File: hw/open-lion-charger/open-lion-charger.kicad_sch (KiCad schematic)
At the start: 5 parts

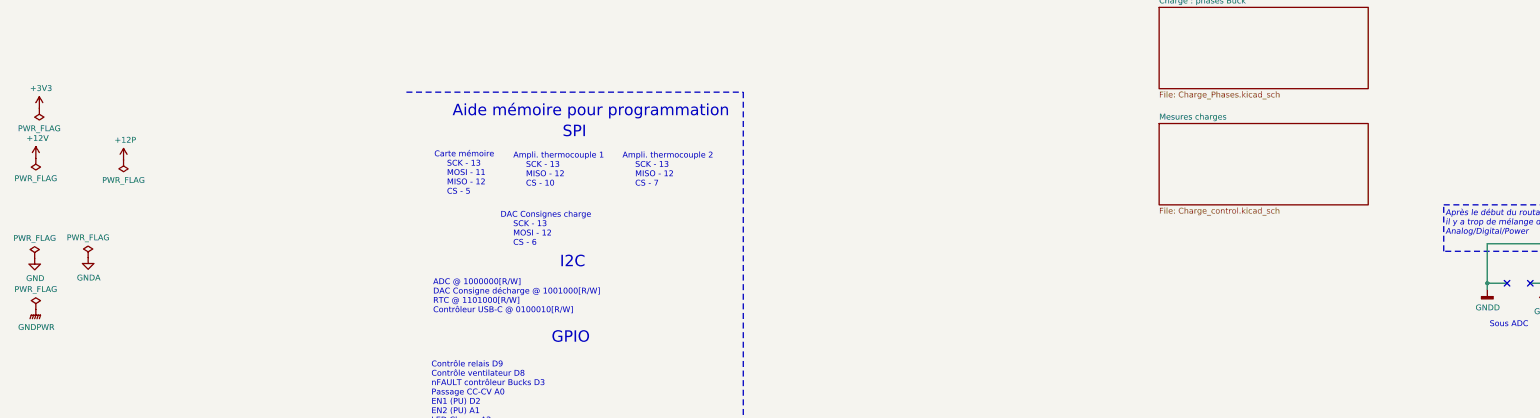
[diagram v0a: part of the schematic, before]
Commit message: Done with PCB review
Warning : issue with net +12P and confusion with RELAIS_BATT_OUT
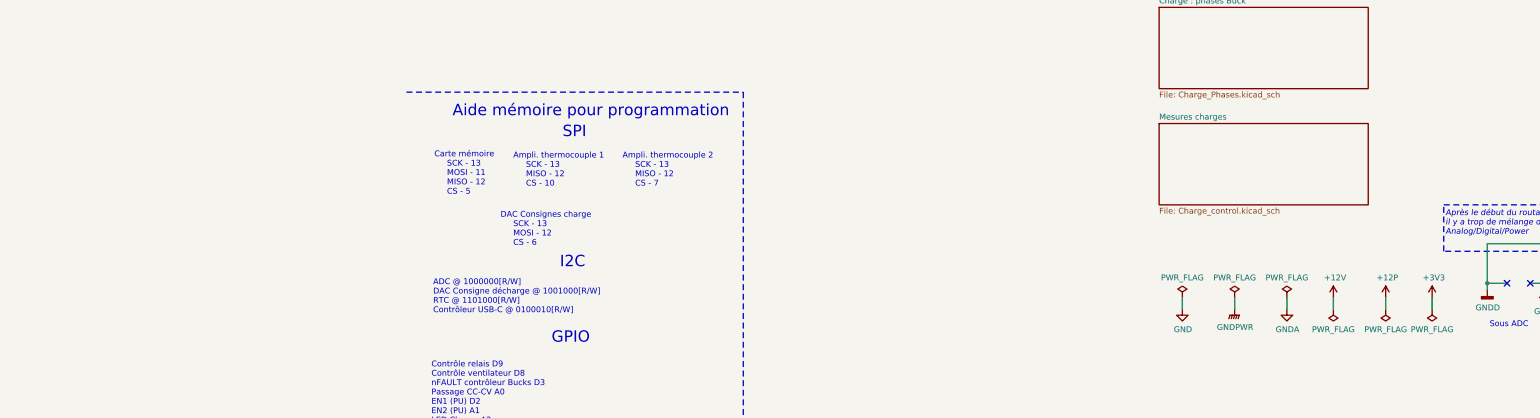
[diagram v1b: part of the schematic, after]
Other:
- company: CHERRIER & PETITJEAN -> (none)
- title: Projet TX54 - A21 - Variant BUCK - Contrôleur LM5170 -> Open LiOn charger

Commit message: Add fab files
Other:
- title: Open LiOn charger -> Open Lithium iOn charger
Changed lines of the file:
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@@
 	(paper "A4")
 	(title_block
-		(title "Open LiOn charger")
+		(title "Open Lithium iOn charger")
 		(rev "B00")
 	)
